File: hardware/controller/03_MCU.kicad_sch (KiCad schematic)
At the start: 4 parts, among them J3 UART recovery / GND, U10 ESP32-S3-WROOM-1-N4

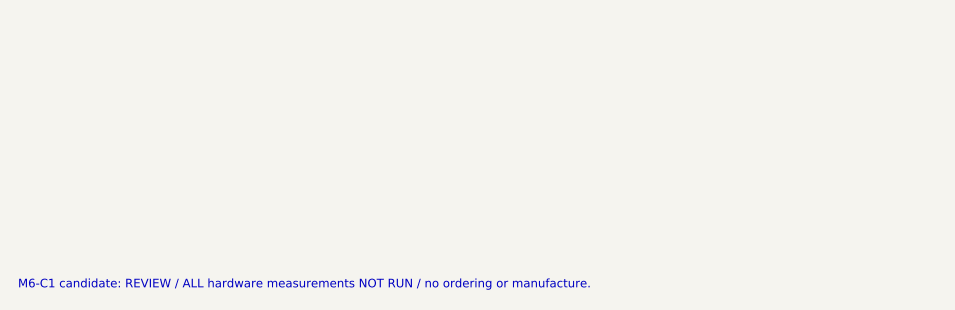
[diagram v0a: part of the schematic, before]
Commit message: M6-C1R1: protect pack identity input and review USB ESD topology
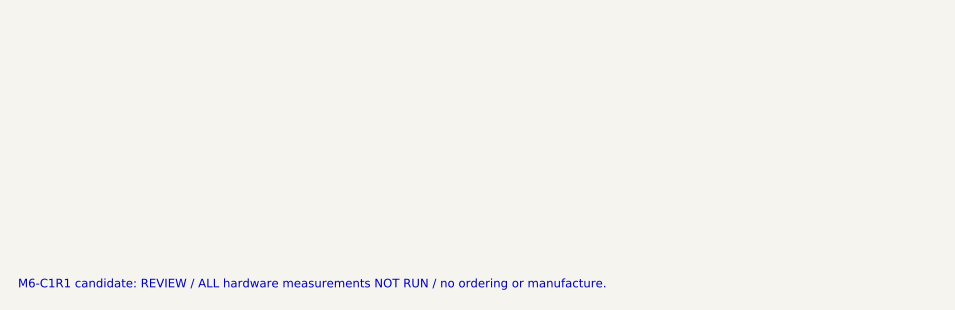
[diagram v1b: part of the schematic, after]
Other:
- note added: "M6-C1R1 candidate: REVIEW / ALL hardware measurements NOT RUN / no ordering or manufacture."
- note removed: "M6-C1 candidate: REVIEW / ALL hardware measurements NOT RUN / no ordering or manufacture."

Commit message: M6-L2 — External antenna, FoxPro2 interface and GPIO expansion
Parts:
- J3: Engineering_Note 3.3V UART, no5V supply. Native USB normal flashing path. St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 -> Default R300/R301 fitted; FoxPro R302/R303 absent. Recovery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
- U10: value ESP32-S3-WROOM-1-N4 -> ESP32-S3-WROOM-1U-N4; footprint ARDF_CTL:ESP32_S3_WROOM_1_Standard -> ARDF_CTL:ESP32_S3_WROOM_1U_N4_L2; Engineering_Note 4MB flash, no PSRAM. GPIO35/36/37 available. GPIO0 boot onl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 -> External2.4GHz antenna only;4MB flash;NO PSRAM. GPIO35..37 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; MPN ESP32-S3-WROOM-1-N4 -> ESP32-S3-WROOM-1U-N4
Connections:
- net UART_RX: no longer J3.3 (3_IO)
- net UART_TX: no longer J3.2 (2_IO)
- net STRAP3: now reaches U10.15 (15_GPIO3)
- net STRAP46: now reaches U10.16 (16_GPIO46)
- new net REC_RX: J3.3 (3_IO)
- new net REC_TX: J3.2 (2_IO)
- no-connect marks 3 -> 1
